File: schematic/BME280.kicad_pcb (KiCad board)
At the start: 2 copper layers, 8.7 x 24 mm, 9 parts, among them J1 Conn_02x04_Odd_Even, U1 BME280, U2 DizzyBITLogo

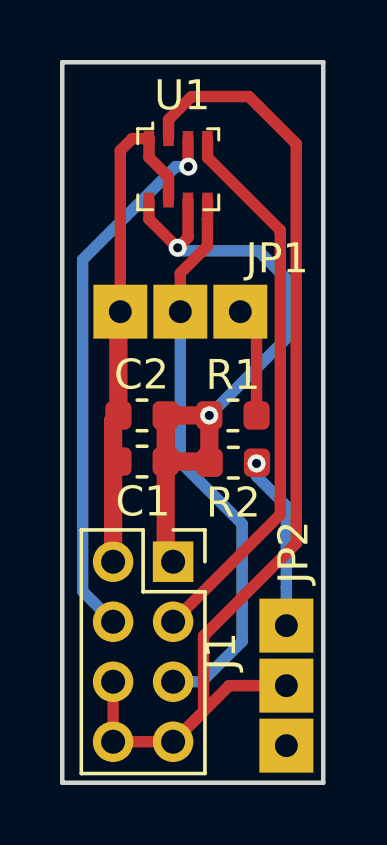
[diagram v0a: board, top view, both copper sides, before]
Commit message: Changed pin numbers
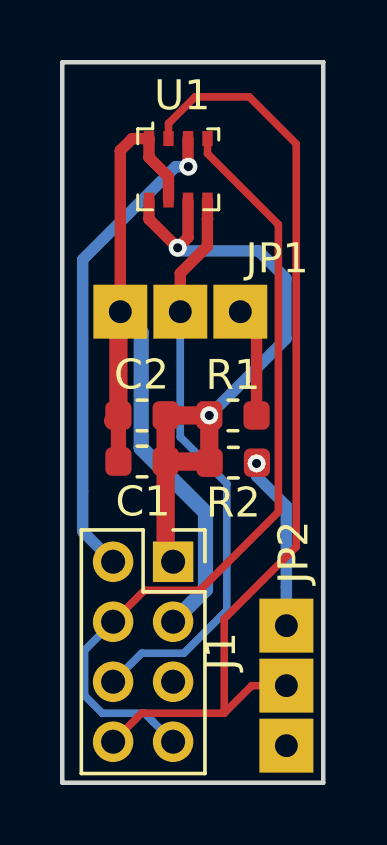
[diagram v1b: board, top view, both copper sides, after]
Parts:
- moved U2 1.80 mm to (104.6, 76.3), turned to 180 degrees
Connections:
- J1 pad 2: GND -> I2C_SDA
- J1 pad 3: SCL -> GND
- J1 pad 4: SDA -> I2C_SCL
- J1 pad 5: SDO_ADDR -> (no net)
- J1 pad 6: CS -> SPI_MISO
- J1 pad 7: CS -> I2C_SCL
- J1 pad 8: CS -> SPI_CS
- JP1 pad 2: SDO_ADDR -> SPI_MISO
- JP2 pad 2: CS -> SPI_CS
- U1 pad 2: CS -> SPI_CS
- U1 pad 3: SDA -> I2C_SDA
- U1 pad 4: SCL -> I2C_SCL
- U1 pad 5: SDO_ADDR -> SPI_MISO
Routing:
- net CS: track 36.0 -> 0.00 mm
- net SPI_CS: track 0.00 -> 32.3 mm
- net I2C_SCL: track 0.00 -> 26.9 mm
- net SPI_MISO: track 0.00 -> 19.5 mm
- net SDO_ADDR: track 18.8 -> 0.00 mm
- net SCL: track 18.6 -> 0.00 mm
- net SDA: track 18.3 -> 0.00 mm, vias 1 -> 0
- net I2C_SDA: track 0.00 -> 16.3 mm, vias 0 -> 1
- net GND: track 17.2 -> 26.0 mm
